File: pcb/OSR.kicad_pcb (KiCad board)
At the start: 2 copper layers, 77.5 x 50.8 mm, 86 parts, among them J1 Conn_01x10_Socket, J10 Conn_01x02_Socket, J11 Conn_01x02_Socket, J12 Conn_01x08_Socket, J13 Conn_01x04_Pin, J15 Conn_01x08_Socket, J2 Conn_01x02_Pin, J3 Conn_01x10_Socket, J4 Conn_02x02_Counter_Clockwise, J5 Conn_02x02_Counter_Clockwise, J6 Conn_02x02_Counter_Clockwise, J7 Conn_02x02_Counter_Clockwise, J8 Conn_02x02_Counter_Clockwise, J9 Conn_02x02_Counter_Clockwise, Q1 BUK7880-55A, Q10 AO3400A, Q11 AO3400A, Q12 AO3400A, Q13 AO3400A, Q14 AO3400A, Q15 AO3400A, Q16 AO3400A, Q17 AO3400A, Q2 MMBFJ113, Q3 MMBFJ113, Q4 MMBFJ113, Q5 MMBFJ113, Q6 MMBFJ113, Q7 MMBFJ113, Q8 MMBFJ113, Q9 MMBFJ113, SW1 SW_SPST, SW2 SW_SPST, U1 4011, U2 40106, U3 HEF4094B

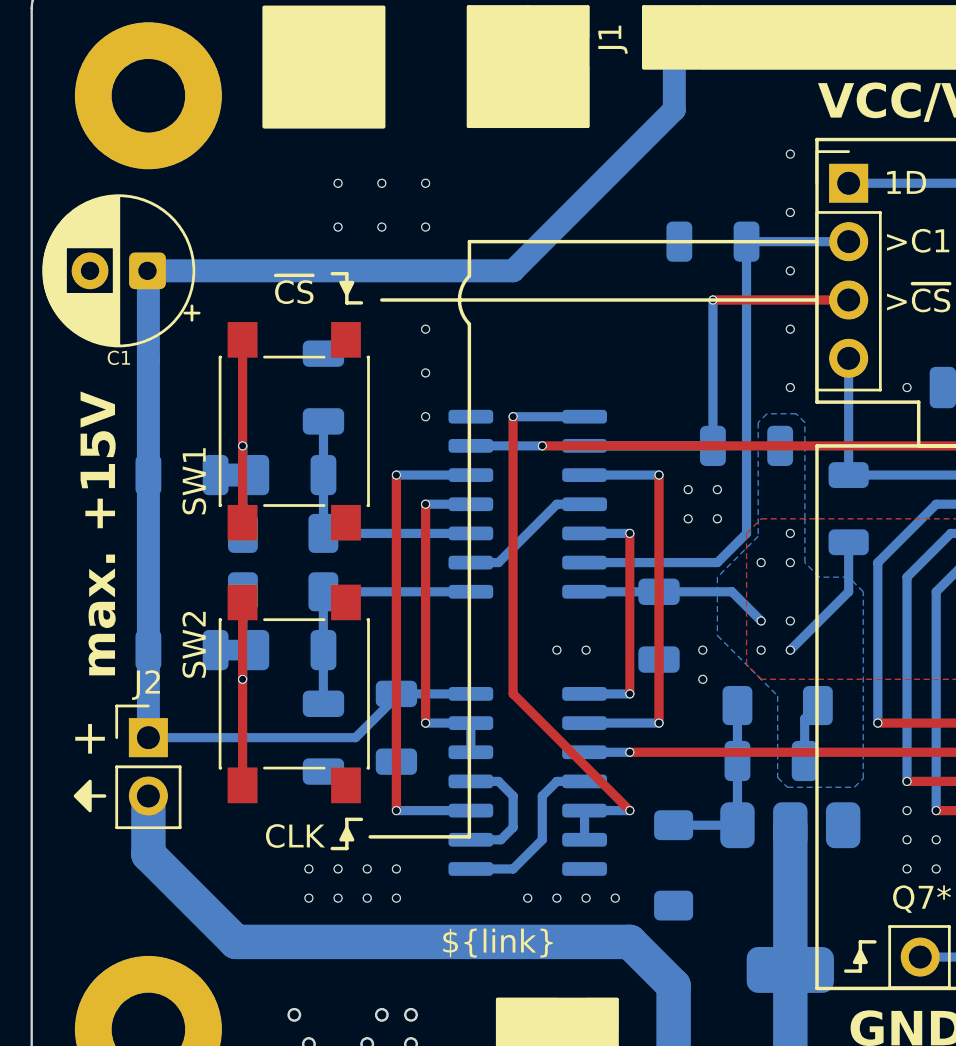
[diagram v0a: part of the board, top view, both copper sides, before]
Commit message: Add CLK and CS led beside push-button
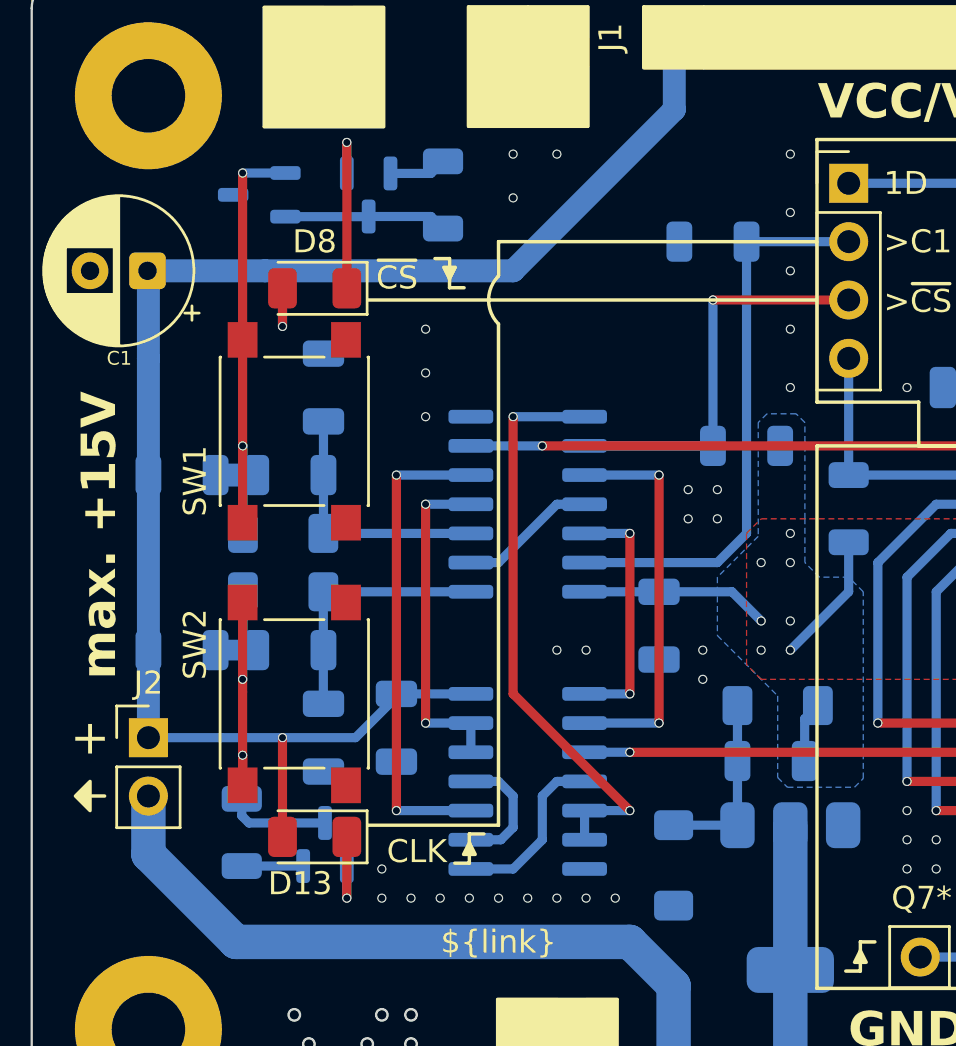
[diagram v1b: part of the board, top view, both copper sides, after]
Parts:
- added D13: Red, LED_SMD:LED_1206_3216Metric, F.Cu at (131.7, 113.5)
- added D8: Red, LED_SMD:LED_1206_3216Metric, F.Cu at (131.7, 89.7)
- added Q18: MMBFJ113, Package_TO_SOT_SMD:SOT-23, B.Cu at (134.0, 85.6)
- added Q19: AO3400A, Package_TO_SOT_SMD:SOT-23-3, B.Cu at (129.3, 85.6)
- added Q20: MMBFJ113, Package_TO_SOT_SMD:SOT-23, B.Cu at (132.1, 113.9)
- added R25: 270, Resistor_SMD:R_1206_3216Metric, B.Cu at (137.3, 85.6)
- added R26: 270, Resistor_SMD:R_1206_3216Metric, B.Cu at (128.5, 113.3)
- moved FID3 0.90 mm to (144.8, 90.8)
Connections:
- net Net-(D11-A) renamed LED_~{CS}
- net Net-(D12-A) renamed LED_CLK
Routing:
- net LED_~{CS}: track 14.0 -> 23.2 mm, vias 1 -> 2
- net VCC: track 110.8 -> 119.5 mm, vias 8 -> 10
- net LED_CLK: track 14.0 -> 21.8 mm, vias 1 -> 2
- net Net-(D8-K): track 0.00 -> 7.70 mm, vias 0 -> 1
- net Net-(Q18-G): track 0.00 -> 7.08 mm
- net Net-(D13-K): track 0.00 -> 4.06 mm, vias 0 -> 1
- net Net-(Q20-S): track 0.00 -> 2.67 mm
- net Net-(Q18-S): track 0.00 -> 2.51 mm
- net GND: vias 84 -> 79

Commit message: Add missing OE text to silkscreen
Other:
- board text added: "OE"
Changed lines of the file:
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@@
+		)
+	)
+	(gr_text "OE"
+		(at 156.464 92.71 0)
+		(layer "F.SilkS")
+		(effects
+			(font
+				(size 1 1)
+				(thickness 0.15)
+			)
+			(justify left)
 		)
 	)
